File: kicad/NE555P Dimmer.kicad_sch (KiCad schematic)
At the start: 7 parts

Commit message: Added new sketches for prototyping and printing
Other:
- moved on the sheet: C2, CT, D?, RA, RV1, U?

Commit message: added Schematics and datasheets
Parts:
- added J1: LED_IN, symbol Connector:Screw_Terminal_01x02
- added Q1: IRF8721PBF-1, Package_SO:SOIC-8_3.9x4.9mm_P1.27mm, symbol Transistor_FET:IRF8721PBF-1
- added R1: 1K5, symbol Device:R
- C2: footprint (none) -> Capacitor_SMD:C_0805_2012Metric
- CT1: renamed from CT; footprint (none) -> Capacitor_SMD:C_0805_2012Metric
- D1: renamed from D?; value 1N4148 -> 1N5189WD; footprint Diode_THT:D_DO-35_SOD27_P7.62mm_Horizontal -> Diode_SMD:D_SOD-323_HandSoldering
- D2: renamed from D?; footprint Diode_THT:D_DO-35_SOD27_P7.62mm_Horizontal -> Diode_SMD:D_SOD-323_HandSoldering
- RA1: renamed from RA; footprint (none) -> Resistor_SMD:R_0805_2012Metric
- RV1: footprint Potentiometer_THT:Potentiometer_Bourns_3005_Horizontal -> Potentiometer_THT:Potentiometer_Piher_T-16H_Single_Horizontal
- U1: renamed from U?; footprint Package_DIP:DIP-8_W7.62mm -> Package_SO:SOIC-8_3.9x4.9mm_P1.27mm
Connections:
- net GND: now also J1.2 (Pin_2), Q1.1 (S), Q1.2 (S), Q1.3 (S)
- net OUT: now also R1.1
- new net: Q1.4 (G), R1.2
- new net LED-: J1.1 (Pin_1), Q1.5 (D), Q1.6 (D), Q1.7 (D), Q1.8 (D)

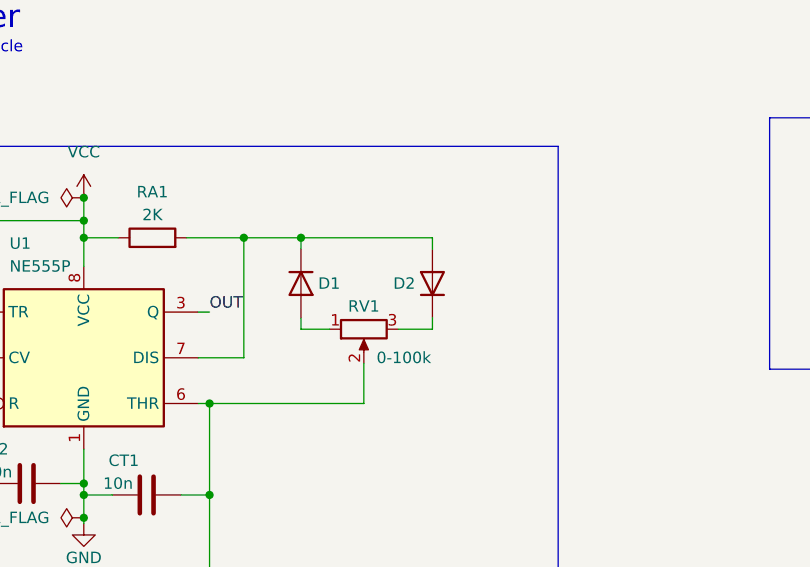
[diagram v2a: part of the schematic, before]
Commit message: Updated schematic with correct diodes
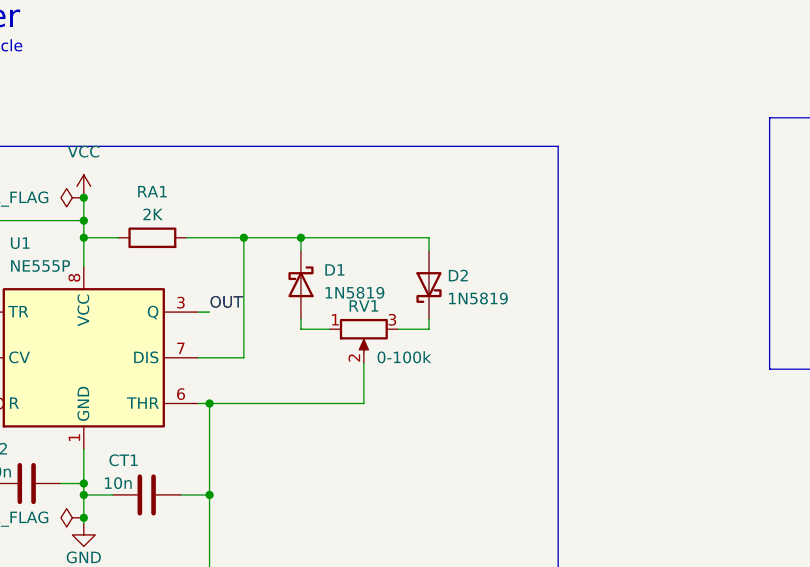
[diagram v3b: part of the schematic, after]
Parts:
- removed D1: 1N5189WD, Diode_SMD:D_SOD-323_HandSoldering, symbol Diode:1N4148
- removed D2: 1N4148, Diode_SMD:D_SOD-323_HandSoldering, symbol Diode:1N4148
- added D1, D2: 1N5819, Diode_THT:D_DO-41_SOD81_P10.16mm_Horizontal, symbol Diode:1N5819
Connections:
- net at RA1.2, U1.7 (DIS): now also D1.1 (K), D2.2 (A)
- net at RV1.1: now also D1.2 (A)
- net at RV1.3: now also D2.1 (K)
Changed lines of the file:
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@@
   (junction (at 57.15 40.64) (diameter 0) (color 0 0 0 0)
   )
+  (junction (at 165.1 53.34) (diameter 0) (color 0 0 0 0)
+  )
+  (junction (at 71.12 63.5) (diameter 0) (color 0 0 0 0)
+  )
+  (junction (at 57.15 72.39) (diameter 0) (color 0 0 0 0)
+  )
+  (junction (at 57.15 76.2) (diameter 0) (color 0 0 0 0)
+  )
+  (junction (at 57.15 73.66) (diameter 0) (color 0 0 0 0)
+  )
+  (junction (at 44.45 63.5) (diameter 0) (color 0 0 0 0)
+  )
   (junction (at 74.93 45.085) (diameter 0) (color 0 0 0 0)
   )
-  (junction (at 165.1 53.34) (diameter 0) (color 0 0 0 0)
-  )
-  (junction (at 71.12 63.5) (diameter 0) (color 0 0 0 0)
-  )
-  (junction (at 57.15 72.39) (diameter 0) (color 0 0 0 0)
-  )
-  (junction (at 57.15 76.2) (diameter 0) (color 0 0 0 0)
-  )
-  (junction (at 57.15 73.66) (diameter 0) (color 0 0 0 0)
-  )
-  (junction (at 44.45 63.5) (diameter 0) (color 0 0 0 0)
+  (junction (at 81.28 45.085) (diameter 0) (color 0 0 0 0)
   )
   (junction (at 57.15 43.18) (diameter 0) (color 0 0 0 0)
@@
   (junction (at 71.12 73.66) (diameter 0) (color 0 0 0 0)
   )
-  (junction (at 81.28 45.085) (diameter 0) (color 0 0 0 0)
-  )
   (junction (at 57.15 45.085) (diameter 0) (color 0 0 0 0)
   )
@@
     (stroke (width 0) (type default) (color 0 0 0 0))
   )
+  (wire (pts (xy 81.28 54.102) (xy 81.28 55.245))
+    (stroke (width 0) (type default) (color 0 0 0 0))
+  )
   (wire (pts (xy 88.265 59.055) (xy 88.265 63.5))
     (stroke (width 0) (type default) (color 0 0 0 0))
@@
     (stroke (width 0) (type default) (color 0 0 0 0))
   )
-  (wire (pts (xy 95.885 53.975) (xy 95.885 55.245))
-    (stroke (width 0) (type default) (color 0 0 0 0))
-  )
   (wire (pts (xy 71.12 83.185) (xy 71.12 73.66))
     (stroke (width 0) (type default) (color 0 0 0 0))
@@
     (stroke (width 0) (type default) (color 0 0 0 0))
   )
-  (wire (pts (xy 81.28 46.355) (xy 81.28 45.085))
-    (stroke (width 0) (type default) (color 0 0 0 0))
-  )
   (wire (pts (xy 171.45 50.8) (xy 176.53 50.8))
     (stroke (width 0) (type default) (color 0 0 0 0))
@@
     (stroke (width 0) (type default) (color 0 0 0 0))
   )
+  (wire (pts (xy 92.075 55.245) (xy 95.504 55.245))
+    (stroke (width 0) (type default) (color 0 0 0 0))
+  )
   (polyline (pts (xy 195.58 59.69) (xy 133.35 59.69))
     (stroke (width 0) (type default) (color 0 0 0 0))
@@
     (stroke (width 0) (type default) (color 0 0 0 0))
   )
-  (wire (pts (xy 95.885 55.245) (xy 92.075 55.245))
-    (stroke (width 0) (type default) (color 0 0 0 0))
-  )
   (wire (pts (xy 57.15 73.66) (xy 57.15 76.2))
     (stroke (width 0) (type default) (color 0 0 0 0))
   )
+  (wire (pts (xy 81.28 45.085) (xy 95.504 45.085))
+    (stroke (width 0) (type default) (color 0 0 0 0))
+  )
   (wire (pts (xy 57.15 45.085) (xy 60.96 45.085))
     (stroke (width 0) (type default) (color 0 0 0 0))
@@
     (stroke (width 0) (type default) (color 0 0 0 0))
   )
-  (wire (pts (xy 95.885 45.085) (xy 81.28 45.085))
-    (stroke (width 0) (type default) (color 0 0 0 0))
-  )
   (wire (pts (xy 57.15 68.58) (xy 57.15 72.39))
     (stroke (width 0) (type default) (color 0 0 0 0))
@@
     (stroke (width 0) (type default) (color 0 0 0 0))
   )
+  (wire (pts (xy 81.28 46.482) (xy 81.28 45.085))
+    (stroke (width 0) (type default) (color 0 0 0 0))
+  )
   (wire (pts (xy 165.1 49.53) (xy 165.1 53.34))
     (stroke (width 0) (type default) (color 0 0 0 0))
@@
     (stroke (width 0) (type default) (color 0 0 0 0))
   )
-  (wire (pts (xy 95.885 46.355) (xy 95.885 45.085))
+  (wire (pts (xy 95.504 45.085) (xy 95.504 46.482))
     (stroke (width 0) (type default) (color 0 0 0 0))
   )
@@
     (stroke (width 0) (type default) (color 0 0 0 0))
   )
-  (wire (pts (xy 81.28 53.975) (xy 81.28 55.245))
-    (stroke (width 0) (type default) (color 0 0 0 0))
-  )
   (wire (pts (xy 44.45 63.5) (xy 44.45 72.39))
+    (stroke (width 0) (type default) (color 0 0 0 0))
+  )
+  (wire (pts (xy 95.504 54.102) (xy 95.504 55.245))
     (stroke (width 0) (type default) (color 0 0 0 0))
   )
@@
     )
     (property "Datasheet" "~" (id 3) (at 64.135 73.66 0)
+      (effects (font (size 1.27 1.27)) hide)
+    )
+    (pin "1")
+    (pin "2")
+  )
+  (symbol (lib_id "Diode:1N5819") (at 81.28 50.292 270) (unit 1)
+    (in_bom yes) (on_board yes) (fields_autoplaced)
+    (property "Reference" "D1" (id 0) (at 83.82 48.7044 90)
+      (effects (font (size 1.27 1.27)) (justify left))
+    )
+    (property "Value" "1N5819" (id 1) (at 83.82 51.2444 90)
+      (effects (font (size 1.27 1.27)) (justify left))
+    )
+    (property "Footprint" "Diode_THT:D_DO-41_SOD81_P10.16mm_Horizontal" (id 2) (at 76.835 50.292 0)
+      (effects (font (size 1.27 1.27)) hide)
+    )
+    (property "Datasheet" "http://www.vishay.com/docs/88525/1n5817.pdf" (id 3) (at 81.28 50.292 0)
       (effects (font (size 1.27 1.27)) hide)
     )
@@
   (symbol (lib_id "power:GND") (at 165.1 55.88 0) (unit 1)
     (in_bom yes) (on_board yes) (fields_autoplaced)
-    (property "Reference" "#PWR?" (id 0) (at 165.1 62.23 0)
+    (property "Reference" "#PWR0101" (id 0) (at 165.1 62.23 0)
       (effects (font (size 1.27 1.27)) hide)
     )
@@
     (pin "1")
   )
-  (symbol (lib_id "Diode:1N4148") (at 81.28 50.165 270) (unit 1)
-    (in_bom yes) (on_board yes)
-    (property "Reference" "D1" (id 0) (at 83.185 50.165 90)
-      (effects (font (size 1.27 1.27)) (justify left))
-    )
-    (property "Value" "1N5189WD" (id 1) (at 83.185 51.435 90)
-      (effects (font (size 1.27 1.27)) (justify left) hide)
-    )
-    (property "Footprint" "Diode_SMD:D_SOD-323_HandSoldering" (id 2) (at 81.28 50.165 0)
-      (effects (font (size 1.27 1.27)) hide)
-    )
-    (property "Datasheet" "https://assets.nexperia.com/documents/data-sheet/1N4148_1N4448.pdf" (id 3) (at 81.28 50.165 0)
+  (symbol (lib_id "Diode:1N5819") (at 95.504 50.292 90) (unit 1)
+    (in_bom yes) (on_board yes) (fields_autoplaced)
+    (property "Reference" "D2" (id 0) (at 97.536 49.3394 90)
+      (effects (font (size 1.27 1.27)) (justify right))
+    )
+    (property "Value" "1N5819" (id 1) (at 97.536 51.8794 90)
+      (effects (font (size 1.27 1.27)) (justify right))
+    )
+    (property "Footprint" "Diode_THT:D_DO-41_SOD81_P10.16mm_Horizontal" (id 2) (at 99.949 50.292 0)
+      (effects (font (size 1.27 1.27)) hide)
+    )
+    (property "Datasheet" "http://www.vishay.com/docs/88525/1n5817.pdf" (id 3) (at 95.504 50.292 0)
       (effects (font (size 1.27 1.27)) hide)
     )
@@
     (pin "2")
   )
-  (symbol (lib_id "Diode:1N4148") (at 95.885 50.165 90) (unit 1)
-    (in_bom yes) (on_board yes)
-    (property "Reference" "D2" (id 0) (at 93.98 50.165 90)
-      (effects (font (size 1.27 1.27)) (justify left))
-    )
-    (property "Value" "1N4148" (id 1) (at 93.98 48.895 90)
-      (effects (font (size 1.27 1.27)) (justify left) hide)
-    )
-    (property "Footprint" "Diode_SMD:D_SOD-323_HandSoldering" (id 2) (at 95.885 50.165 0)
-      (effects (font (size 1.27 1.27)) hide)
-    )
-    (property "Datasheet" "https://assets.nexperia.com/documents/data-sheet/1N4148_1N4448.pdf" (id 3) (at 95.885 50.165 0)
-      (effects (font (size 1.27 1.27)) hide)
-    )
-    (pin "1")
-    (pin "2")
-  )
   (sheet_instances
     (path "/" (page "1"))
@@
     )
     (path "/6ee24c30-57f8-4c8a-9156-0f947ed91087"
-      (reference "#PWR?") (unit 1) (value "GND") (footprint "")
+      (reference "#PWR0101") (unit 1) (value "GND") (footprint "")
     )
     (path "/8555c02b-78f4-4200-9ab9-931035464136"
@@
       (reference "CT1") (unit 1) (value "10n") (footprint "Capacitor_SMD:C_0805_2012Metric")
     )
-    (path "/c1c0bc07-6297-4907-ab1f-2637d13c9b94"
-      (reference "D1") (unit 1) (value "1N5189WD") (footprint "Diode_SMD:D_SOD-323_HandSoldering")
-    )
-    (path "/d6647dbf-660a-4483-9b20-89bafda63569"
-      (reference "D2") (unit 1) (value "1N4148") (footprint "Diode_SMD:D_SOD-323_HandSoldering")
+    (path "/16534c7b-2b1c-4bbb-8017-d277a73da324"
+      (reference "D1") (unit 1) (value "1N5819") (footprint "Diode_THT:D_DO-41_SOD81_P10.16mm_Horizontal")
+    )
+    (path "/c18d5988-1b90-4ff5-aa6d-8b46027adf8b"
+      (reference "D2") (unit 1) (value "1N5819") (footprint "Diode_THT:D_DO-41_SOD81_P10.16mm_Horizontal")
     )
     (path "/1d796605-c3cc-4927-aebe-41bd091cd38c"
